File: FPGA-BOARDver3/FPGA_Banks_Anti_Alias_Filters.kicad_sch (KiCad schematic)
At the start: 10 parts, among them U1 XC7Z020-1CLG400I__

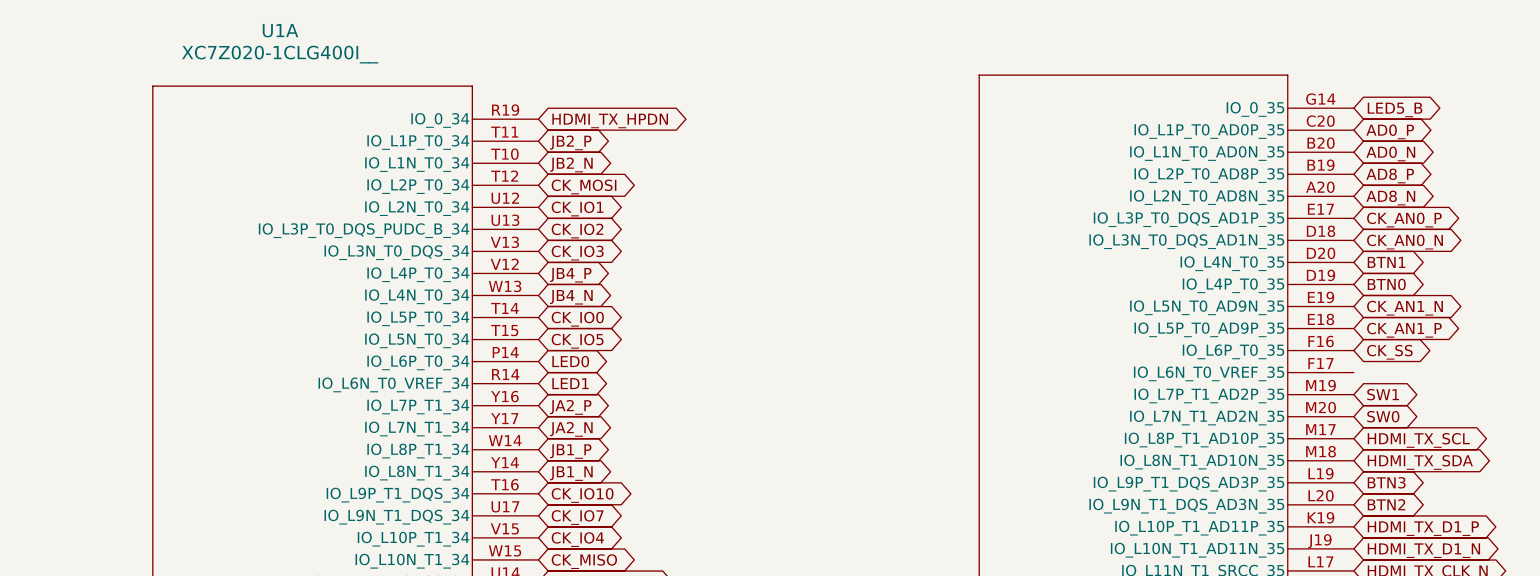
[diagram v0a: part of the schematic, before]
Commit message: All pages complete , pi header left
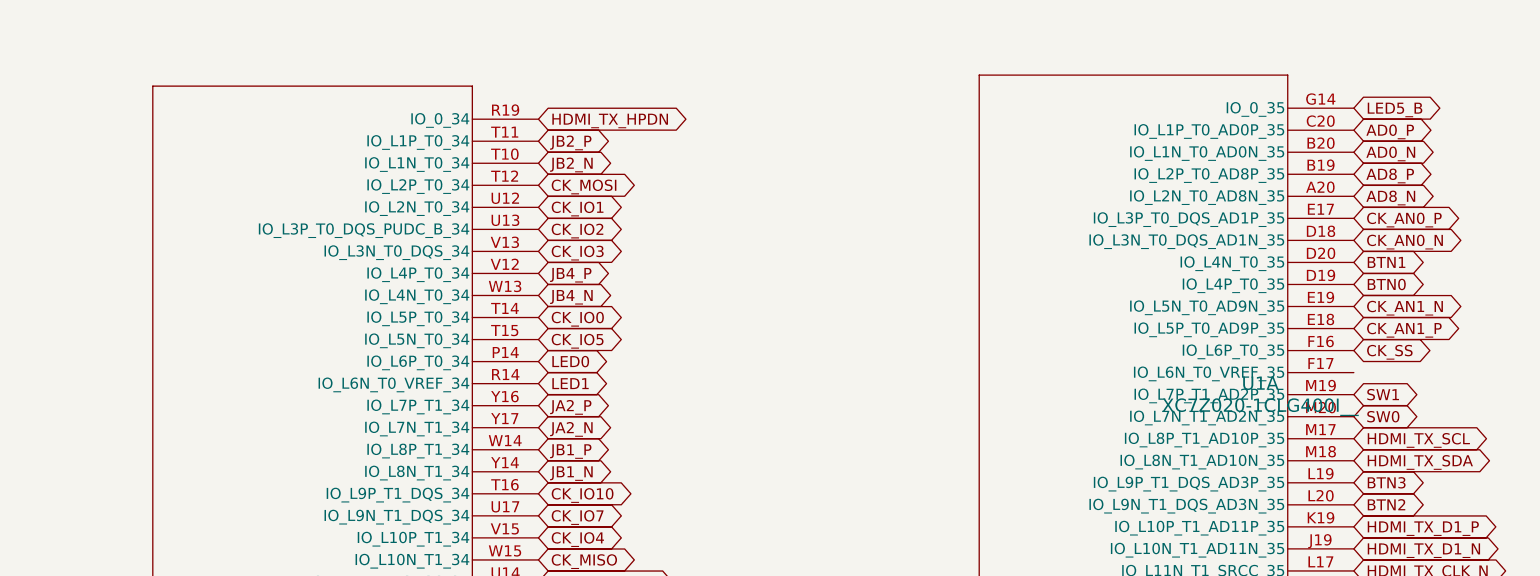
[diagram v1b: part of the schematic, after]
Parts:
- C1, C2, C3: footprint Capacitor_SMD:C_0402_1005Metric -> footprints:C_0402
- U1: footprint XC7Z020-1CLG400I:CLG400_ZYNQ-7000_AMD -> footprints:CLG400_ZYNQ-7000_AMD
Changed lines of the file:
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@@
 			)
 		)
-		(property "Footprint" "Capacitor_SMD:C_0402_1005Metric"
+		(property "Footprint" "footprints:C_0402"
 			(at 41.6052 180.34 0)
 			(effects
@@
 			)
 		)
-		(property "Footprint" "Capacitor_SMD:C_0402_1005Metric"
+		(property "Footprint" "footprints:C_0402"
 			(at 41.6052 142.24 0)
 			(effects
@@
 		(fields_autoplaced yes)
 		(property "Reference" "U1"
-			(at 141.6367 15.24 0)
+			(at 254.635 55.88 0)
 			(effects
 				(font
@@
 		)
 		(property "Value" "XC7Z020-1CLG400I__"
-			(at 141.6367 17.78 0)
+			(at 254.635 58.42 0)
 			(effects
 				(font
@@
 			)
 		)
-		(property "Footprint" "XC7Z020-1CLG400I:CLG400_ZYNQ-7000_AMD"
+		(property "Footprint" "footprints:CLG400_ZYNQ-7000_AMD"
 			(at 240.538 -5.08 0)
 			(effects
@@
 			(project ""
 				(path "/4a327bdf-04e5-4836-9c0a-5fb801c23f64/19a3c51a-4800-4c20-b3a0-7667316cb050"
+					(reference "U1")
+					(unit 1)
+				)
+				(path "/4a327bdf-04e5-4836-9c0a-5fb801c23f64/41e60eaf-6223-4c1c-9aff-98af239c75fe"
 					(reference "U1")
 					(unit 1)
@@
 			)
 		)
-		(property "Footprint" "Capacitor_SMD:C_0402_1005Metric"
+		(property "Footprint" "footprints:C_0402"
 			(at 41.6052 160.02 0)
 			(effects

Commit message: update
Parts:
- added R189: 4.7K, footprints:R_0402, symbol Device:R_US
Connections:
- net CK_IO2: now also R189.1
- new net +3V3: R189.2
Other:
- note added: "BANK 13"
- note added: "BANK 34"
- note added: "BANK 35"
- note added: "VCC3V3"

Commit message: schematic pages for review
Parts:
- removed R189: 4.7K, footprints:R_0402, symbol Device:R_US
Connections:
- net CK_AN0_N renamed GPIO_25
- net CK_AN0_P renamed GPIO_24
- net CK_AN1_N renamed GPIO_1(EEPROM_SCL)
- net CK_AN1_P renamed GPIO_7(SPI0_CE1)
- net CK_AN2_N renamed SPDIF_TX
- net CK_AN2_P renamed SPDIF_RX
- net CK_AN4_N renamed GPIO_16
- net CK_AN4_P renamed GPIO_12(PWM0)
- net CK_AN5_N renamed GPIO_21(PCM_DOUT)
- net CK_AN5_P renamed GPIO_20(PCM_DIN)
- net CK_IO0 renamed GPIO_17
- net CK_IO1 renamed GPIO_18(PCM_CLK)
- net CK_IO10 renamed GPIO_22
- net CK_IO11 renamed GPIO_13(PWM1)
- net CK_IO12 renamed GPIO_15(UART_RX)
- net CK_IO13 renamed GPIO_14(UART_TX)
- net CK_IO2 renamed GPIO_23
- net CK_IO3 renamed GPIO_4(GPCLK0)
- net CK_IO4 renamed GPIO_5
- net CK_IO5 renamed GPIO_27
- net CK_IO6 renamed GPIO_6
- net CK_IO7 renamed GPIO_0(EEPROM_SDA)
- net CK_IO8 renamed GPIO_19(PCM_FS)
- net CK_IO9 renamed GPIO_26
- net CK_MISO renamed GPIO_9(SPI_MISO)
- net CK_MOSI renamed GPIO_10(SPI_MOSI)
- net CK_SCK renamed GPIO_11(SPI0_SCLK)
- net CK_SCL renamed GPIO_3(I2C1_SCL)
- net CK_SDA renamed GPIO_2(I2C1_SDA)
- net CK_SS renamed GPIO_8(SPI0_CE0)

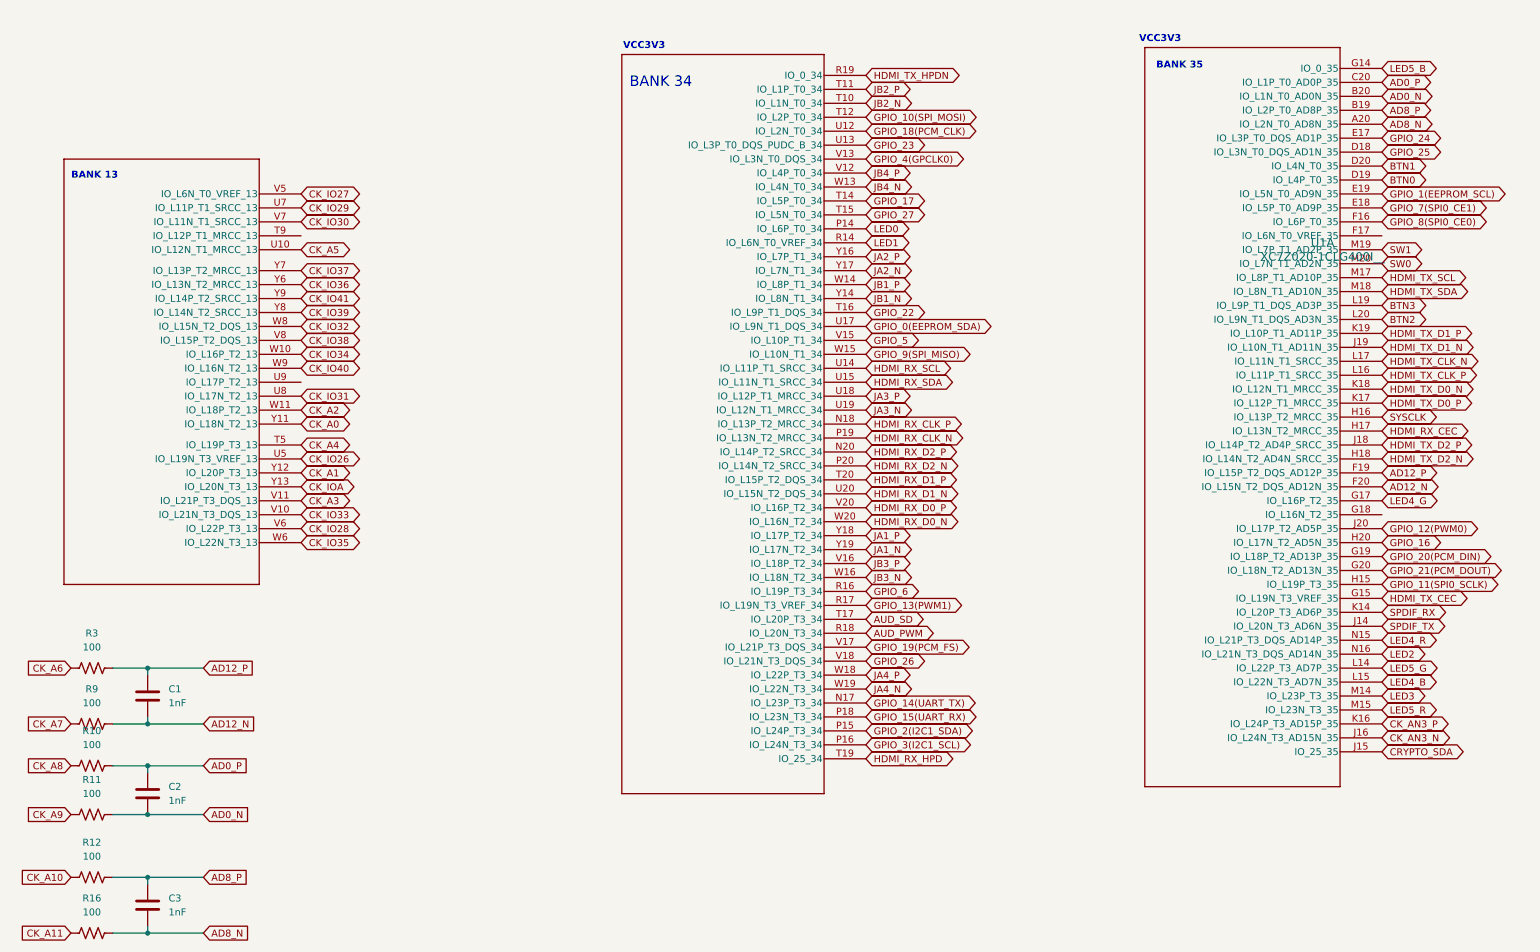
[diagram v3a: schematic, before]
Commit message: Schematic update for review
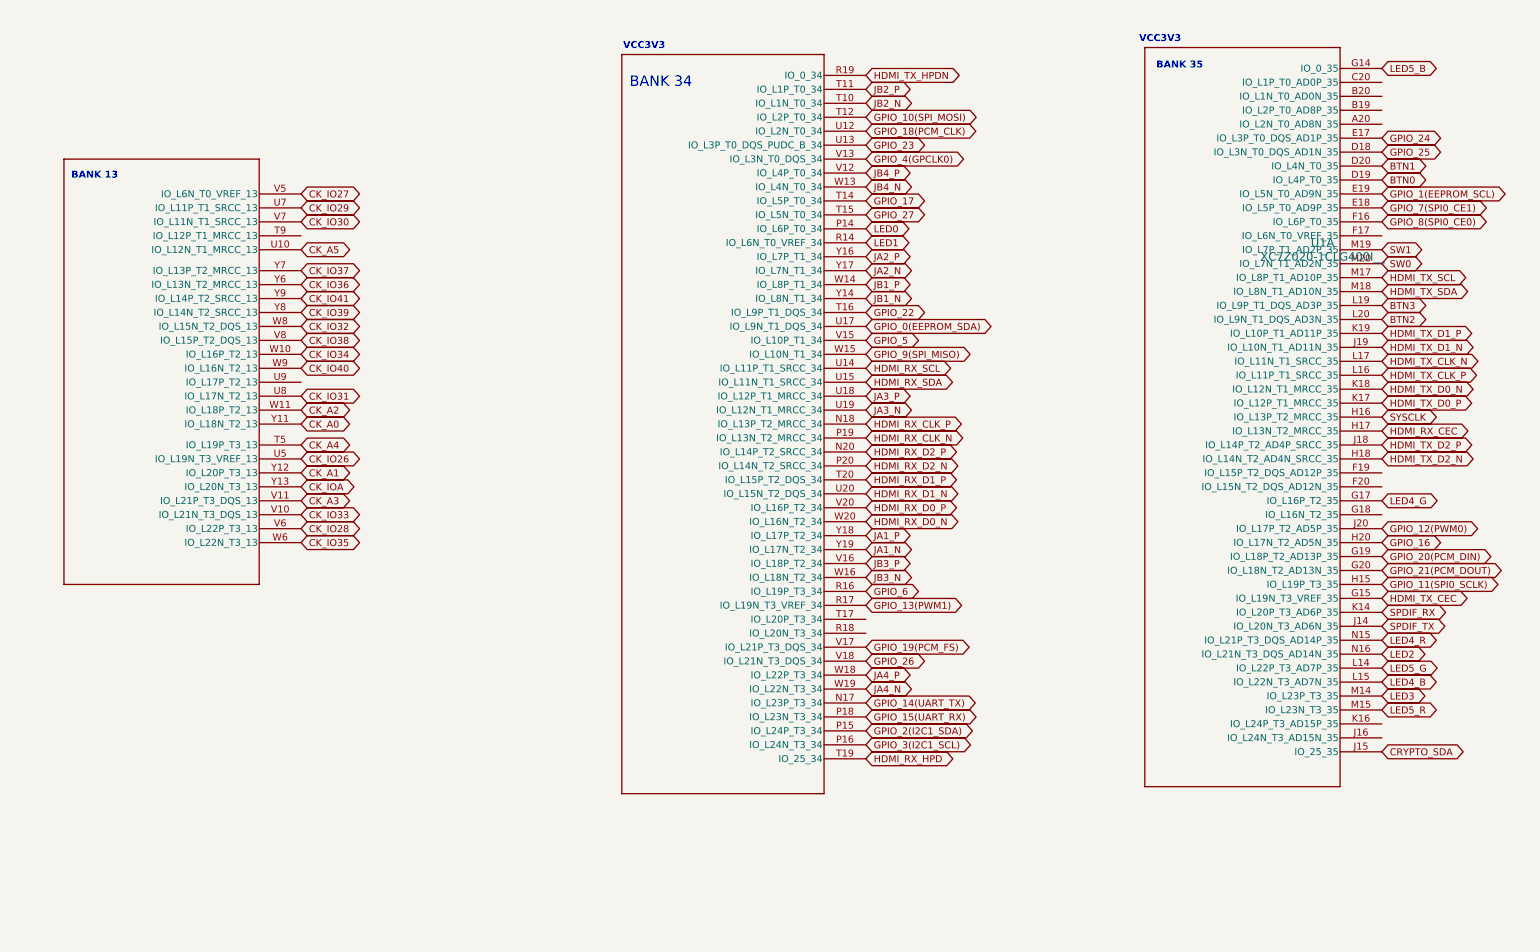
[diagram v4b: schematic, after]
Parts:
- removed C1, C2, C3: 1nF, footprints:C_0402, symbol Device:C
- removed R10, R11, R12, R16, R3, R9: 100, footprints:R_0402, symbol Device:R_US
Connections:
- net AD0_N: no longer names the net of U1.B20 (IO_L1N_T0_AD0N_35)
- net AD0_P: no longer names the net of U1.C20 (IO_L1P_T0_AD0P_35)
- net AD12_N: no longer names the net of U1.F20 (IO_L15N_T2_DQS_AD12N_35)
- net AD12_P: no longer names the net of U1.F19 (IO_L15P_T2_DQS_AD12P_35)
- net AD8_N: no longer names the net of U1.A20 (IO_L2N_T0_AD8N_35)
- net AD8_P: no longer names the net of U1.B19 (IO_L2P_T0_AD8P_35)
- net AUD_PWM: no longer names the net of U1.R18 (IO_L20N_T3_34)
- net AUD_SD: no longer names the net of U1.T17 (IO_L20P_T3_34)
- net CK_AN3_N: no longer names the net of U1.J16 (IO_L24N_T3_AD15N_35)
- net CK_AN3_P: no longer names the net of U1.K16 (IO_L24P_T3_AD15P_35)

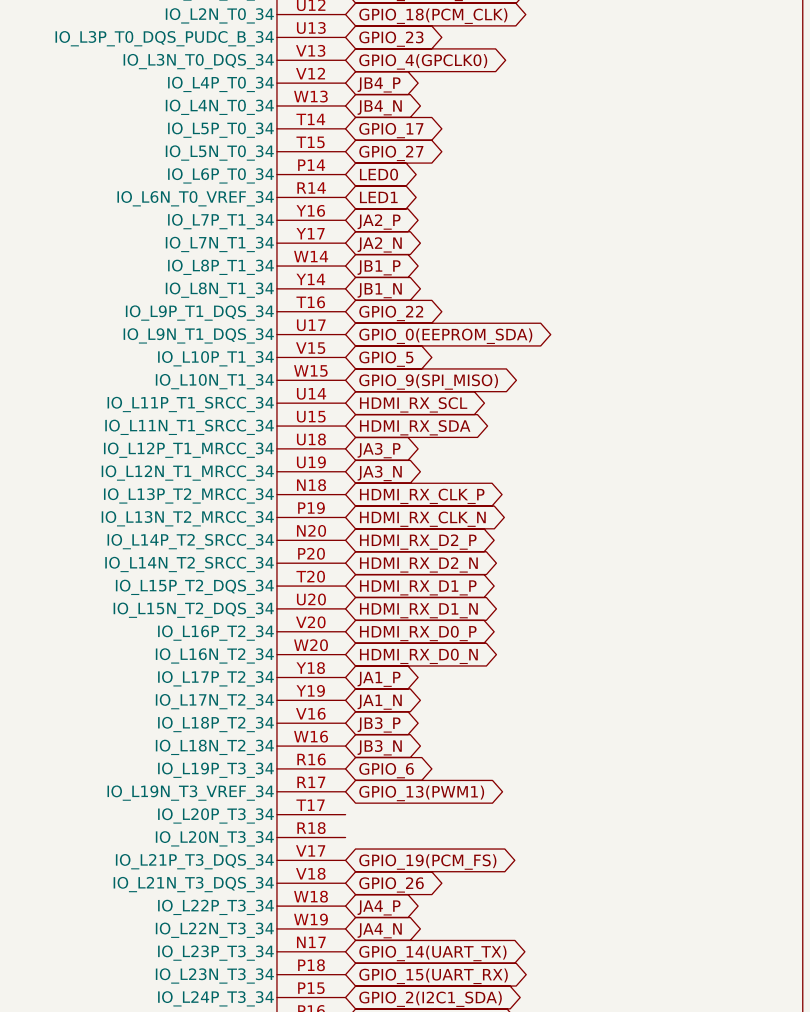
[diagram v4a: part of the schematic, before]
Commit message: added audio out and usb
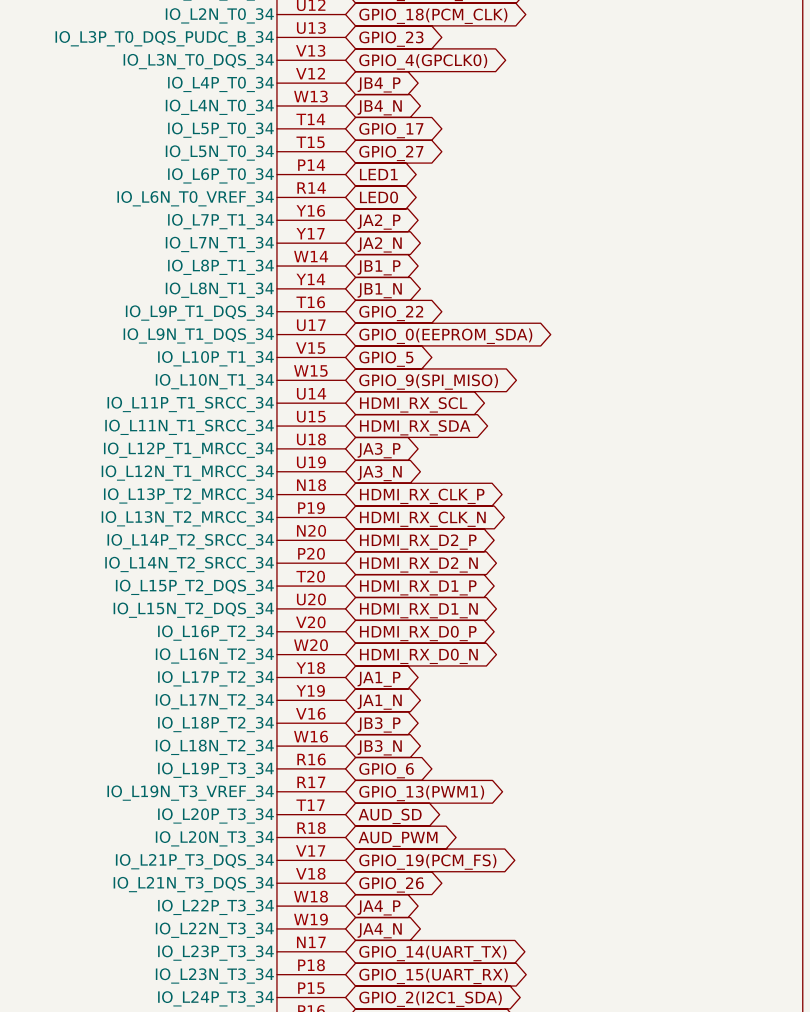
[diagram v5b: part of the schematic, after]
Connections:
- net LED0: now also U1.R14 (IO_L6N_T0_VREF_34); no longer U1.P14 (IO_L6P_T0_34)
- net LED1: now also U1.P14 (IO_L6P_T0_34); no longer U1.R14 (IO_L6N_T0_VREF_34)
- net AUD_PWM: now reaches U1.R18 (IO_L20N_T3_34)
- net AUD_SD: now reaches U1.T17 (IO_L20P_T3_34)
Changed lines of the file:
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@@
+		)
+	)
+	(global_label "AUD_SD"
+		(shape bidirectional)
+		(at 171.45 124.46 0)
+		(fields_autoplaced yes)
+		(effects
+			(font
+				(size 1.27 1.27)
+			)
+			(justify left)
+		)
+		(property "Intersheetrefs" "${INTERSHEET_REFS}"
+			(at 182.6827 124.46 0)
+			(effects
+				(font
+					(size 1.27 1.27)
+				)
+				(justify left)
+				(hide yes)
+			)
 		)
 	)
@@
 		)
 	)
+	(global_label "LED0"
+		(shape bidirectional)
+		(at 171.45 55.88 0)
+		(fields_autoplaced yes)
+		(effects
+			(font
+				(size 1.27 1.27)
+			)
+			(justify left)
+		)
+		(property "Intersheetrefs" "${INTERSHEET_REFS}"
+			(at 180.2031 55.88 0)
+			(effects
+				(font
+					(size 1.27 1.27)
+				)
+				(justify left)
+				(hide yes)
+			)
+		)
+	)
+	(global_label "BTN3"
+		(shape bidirectional)
+		(at 265.43 67.31 0)
+		(fields_autoplaced yes)
+		(effects
+			(font
+				(size 1.27 1.27)
+			)
+			(justify left)
+		)
+		(property "Intersheetrefs" "${INTERSHEET_REFS}"
+			(at 274.3041 67.31 0)
+			(effects
+				(font
+					(size 1.27 1.27)
+				)
+				(justify left)
+				(hide yes)
+			)
+		)
+	)
+	(global_label "HDMI_RX_D0_P"
+		(shape bidirectional)
+		(at 171.45 104.14 0)
+		(fields_autoplaced yes)
+		(effects
+			(font
+				(size 1.27 1.27)
+			)
+			(justify left)
+		)
+		(property "Intersheetrefs" "${INTERSHEET_REFS}"
+			(at 189.335 104.14 0)
+			(effects
+				(font
+					(size 1.27 1.27)
+				)
+				(justify left)
+				(hide yes)
+			)
+		)
+	)
 	(global_label "LED1"
 		(shape bidirectional)
-		(at 171.45 55.88 0)
-		(fields_autoplaced yes)
-		(effects
-			(font
-				(size 1.27 1.27)
-			)
-			(justify left)
-		)
-		(property "Intersheetrefs" "${INTERSHEET_REFS}"
-			(at 180.2031 55.88 0)
-			(effects
-				(font
-					(size 1.27 1.27)
-				)
-				(justify left)
-				(hide yes)
-			)
-		)
-	)
-	(global_label "BTN3"
-		(shape bidirectional)
-		(at 265.43 67.31 0)
-		(fields_autoplaced yes)
-		(effects
-			(font
-				(size 1.27 1.27)
-			)
-			(justify left)
-		)
-		(property "Intersheetrefs" "${INTERSHEET_REFS}"
-			(at 274.3041 67.31 0)
-			(effects
-				(font
-					(size 1.27 1.27)
-				)
-				(justify left)
-				(hide yes)
-			)
-		)
-	)
-	(global_label "HDMI_RX_D0_P"
-		(shape bidirectional)
-		(at 171.45 104.14 0)
-		(fields_autoplaced yes)
-		(effects
-			(font
-				(size 1.27 1.27)
-			)
-			(justify left)
-		)
-		(property "Intersheetrefs" "${INTERSHEET_REFS}"
-			(at 189.335 104.14 0)
-			(effects
-				(font
-					(size 1.27 1.27)
-				)
-				(justify left)
-				(hide yes)
-			)
-		)
-	)
-	(global_label "LED0"
-		(shape bidirectional)
 		(at 171.45 53.34 0)
 		(fields_autoplaced yes)
@@
 		(property "Intersheetrefs" "${INTERSHEET_REFS}"
 			(at 80.5384 110.49 0)
+			(effects
+				(font
+					(size 1.27 1.27)
+				)
+				(justify left)
+				(hide yes)
+			)
+		)
+	)
+	(global_label "AUD_PWM"
+		(shape bidirectional)
+		(at 171.45 127 0)
+		(fields_autoplaced yes)
+		(effects
+			(font
+				(size 1.27 1.27)
+			)
+			(justify left)
+		)
+		(property "Intersheetrefs" "${INTERSHEET_REFS}"
+			(at 184.376 127 0)
 			(effects
 				(font
@@
 			(effects
 				(font
+					(size 1.27 1.27)
+				)
+				(hide yes)
+			)
+		)
+		(property "lcsc#" ""
+			(at 207.01 72.39 0)
+			(effects
+				(font
